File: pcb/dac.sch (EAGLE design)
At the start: 24 parts, among them Q1 2N7000, U1 PIC16F1773-I/SP, U2 MCP6002-I/P

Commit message: Notes on diffusion angle and lighting
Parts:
- removed R3: 220R, rcl:R-US_0207/2V
- added R5, RP: 100R, rcl:R-US_0207/2V
- JPH: device pinhead:PINHD-1X4 -> pinhead:PINHD-1X5
- R1, R2, R4: value 220R -> 100R
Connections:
- new net N$1: JPH.5, RP.2
- net +5V: now also R5.1, RP.1; no longer R3.1
- net LED3: now also R4.2; no longer R3.2
- net LED4: now also R5.2; no longer R4.2
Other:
- note added: "105mA < 200mA"
- note added: "R1-R5: C5xx-Axx amber LEDs Rp: C5xx-Rxx red LED If ~ 21mA < 30mA Vf = 2.1V typ"
- note removed: "53mA < 200mA"
- note removed: "LTL-1CHA amber LEDs If ~ 13mA < 20mA Vf = 2.1V typ"
- moved on the sheet: R4
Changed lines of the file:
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@@
 <?xml version="1.0" encoding="utf-8"?>
 <!DOCTYPE eagle SYSTEM "eagle.dtd">
-<eagle version="9.6.2">
+<eagle version="9.5.2">
 <drawing>
 <settings>
@@
 <part name="GND6" library="supply1" library_urn="urn:adsk.eagle:library:371" deviceset="GND" device=""/>
 <part name="P+4" library="supply1" library_urn="urn:adsk.eagle:library:371" deviceset="+5V" device=""/>
-<part name="R1" library="rcl" library_urn="urn:adsk.eagle:library:334" deviceset="R-US_" device="0207/2V" package3d_urn="urn:adsk.eagle:package:23490/1" value="220R"/>
-<part name="R2" library="rcl" library_urn="urn:adsk.eagle:library:334" deviceset="R-US_" device="0207/2V" package3d_urn="urn:adsk.eagle:package:23490/1" value="220R"/>
-<part name="R3" library="rcl" library_urn="urn:adsk.eagle:library:334" deviceset="R-US_" device="0207/2V" package3d_urn="urn:adsk.eagle:package:23490/1" value="220R"/>
-<part name="R4" library="rcl" library_urn="urn:adsk.eagle:library:334" deviceset="R-US_" device="0207/2V" package3d_urn="urn:adsk.eagle:package:23490/1" value="220R"/>
+<part name="R1" library="rcl" library_urn="urn:adsk.eagle:library:334" deviceset="R-US_" device="0207/2V" package3d_urn="urn:adsk.eagle:package:23490/1" value="100R"/>
+<part name="R2" library="rcl" library_urn="urn:adsk.eagle:library:334" deviceset="R-US_" device="0207/2V" package3d_urn="urn:adsk.eagle:package:23490/1" value="100R"/>
+<part name="R4" library="rcl" library_urn="urn:adsk.eagle:library:334" deviceset="R-US_" device="0207/2V" package3d_urn="urn:adsk.eagle:package:23490/1" value="100R"/>
+<part name="R5" library="rcl" library_urn="urn:adsk.eagle:library:334" deviceset="R-US_" device="0207/2V" package3d_urn="urn:adsk.eagle:package:23490/1" value="100R"/>
 <part name="Q1" library="transistor-fet" library_urn="urn:adsk.eagle:library:396" deviceset="TN0604N3" device="" package3d_urn="urn:adsk.eagle:package:28535/2" value="2N7000"/>
 <part name="GND7" library="supply1" library_urn="urn:adsk.eagle:library:371" deviceset="GND" device=""/>
@@
 <part name="GND10" library="supply1" library_urn="urn:adsk.eagle:library:371" deviceset="GND" device=""/>
 <part name="JPL" library="pinhead" library_urn="urn:adsk.eagle:library:325" deviceset="PINHD-1X3" device="" package3d_urn="urn:adsk.eagle:package:22458/2"/>
-<part name="JPH" library="pinhead" library_urn="urn:adsk.eagle:library:325" deviceset="PINHD-1X4" device="" package3d_urn="urn:adsk.eagle:package:22407/2"/>
+<part name="JPH" library="pinhead" library_urn="urn:adsk.eagle:library:325" deviceset="PINHD-1X5" device="" package3d_urn="urn:adsk.eagle:package:22469/2"/>
 <part name="D1" library="diode" library_urn="urn:adsk.eagle:library:210" deviceset="ZENER-DIODE" device="P1-Z12" package3d_urn="urn:adsk.eagle:package:43340/1" value="SA5.0A"/>
 <part name="JG1H" library="pinhead" library_urn="urn:adsk.eagle:library:325" deviceset="PINHD-1X1" device="" package3d_urn="urn:adsk.eagle:package:22485/2"/>
@@
 <part name="JG5H" library="pinhead" library_urn="urn:adsk.eagle:library:325" deviceset="PINHD-1X1" device="" package3d_urn="urn:adsk.eagle:package:22485/2"/>
 <part name="JG5L" library="pinhead" library_urn="urn:adsk.eagle:library:325" deviceset="PINHD-1X1" device="" package3d_urn="urn:adsk.eagle:package:22485/2"/>
+<part name="RP" library="rcl" library_urn="urn:adsk.eagle:library:334" deviceset="R-US_" device="0207/2V" package3d_urn="urn:adsk.eagle:package:23490/1" value="100R"/>
 </parts>
 <sheets>
@@
 <text x="134.62" y="142.24" size="1.778" layer="97">Connect to something like the Adafruit 206 cable,
 crimp female rectangular cable</text>
-<text x="127" y="92.71" size="1.778" layer="97">LTL-1CHA amber LEDs
-If ~ 13mA &lt; 20mA
+<text x="132.08" y="99.06" size="1.778" layer="97" rot="MR180">R1-R5: C5xx-Axx amber LEDs
+Rp: C5xx-Rxx red LED
+If ~ 21mA &lt; 30mA
 Vf = 2.1V typ</text>
-<text x="109.22" y="100.33" size="1.778" layer="97" rot="MR0">53mA &lt; 200mA</text>
+<text x="109.22" y="100.33" size="1.778" layer="97" rot="MR0">105mA &lt; 200mA</text>
 </plain>
 <instances>
@@
 <attribute name="VALUE" x="150.368" y="121.92" size="1.778" layer="96" rot="R270"/>
 </instance>
-<instance part="R3" gate="G$1" x="153.67" y="120.65" smashed="yes" rot="R270">
+<instance part="R4" gate="G$1" x="153.67" y="120.65" smashed="yes" rot="R270">
 <attribute name="NAME" x="155.1686" y="127" size="1.778" layer="95" rot="R270"/>
 <attribute name="VALUE" x="155.448" y="121.92" size="1.778" layer="96" rot="R270"/>
 </instance>
-<instance part="R4" gate="G$1" x="158.75" y="120.65" smashed="yes" rot="R270">
+<instance part="R5" gate="G$1" x="158.75" y="120.65" smashed="yes" rot="R270">
 <attribute name="NAME" x="160.2486" y="127" size="1.778" layer="95" rot="R270"/>
 <attribute name="VALUE" x="160.528" y="121.92" size="1.778" layer="96" rot="R270"/>
@@
 </instance>
 <instance part="JPL" gate="A" x="128.27" y="110.49" smashed="yes">
-<attribute name="NAME" x="121.92" y="118.745" size="1.778" layer="95"/>
+<attribute name="NAME" x="121.92" y="116.205" size="1.778" layer="95"/>
 <attribute name="VALUE" x="121.92" y="102.87" size="1.778" layer="96"/>
 </instance>
@@
 <attribute name="NAME" x="68.58" y="26.035" size="1.778" layer="95" rot="R180"/>
 <attribute name="VALUE" x="77.47" y="30.48" size="1.778" layer="96" rot="R180"/>
+</instance>
+<instance part="RP" gate="G$1" x="163.83" y="120.65" smashed="yes" rot="R270">
+<attribute name="NAME" x="165.3286" y="127" size="1.778" layer="95" rot="R270"/>
+<attribute name="VALUE" x="165.608" y="121.92" size="1.778" layer="96" rot="R270"/>
 </instance>
 </instances>
@@
 <pinref part="R1" gate="G$1" pin="1"/>
 <wire x1="143.51" y1="128.27" x2="143.51" y2="127" width="0.1524" layer="91"/>
-<pinref part="R4" gate="G$1" pin="1"/>
+<pinref part="R5" gate="G$1" pin="1"/>
 <wire x1="143.51" y1="127" x2="143.51" y2="125.73" width="0.1524" layer="91"/>
 <wire x1="158.75" y1="125.73" x2="158.75" y2="127" width="0.1524" layer="91"/>
@@
 <wire x1="148.59" y1="125.73" x2="148.59" y2="127" width="0.1524" layer="91"/>
 <junction x="148.59" y="127"/>
-<pinref part="R3" gate="G$1" pin="1"/>
+<pinref part="R4" gate="G$1" pin="1"/>
 <wire x1="153.67" y1="125.73" x2="153.67" y2="127" width="0.1524" layer="91"/>
 <junction x="153.67" y="127"/>
+<pinref part="RP" gate="G$1" pin="1"/>
+<wire x1="163.83" y1="125.73" x2="163.83" y2="127" width="0.1524" layer="91"/>
+<wire x1="163.83" y1="127" x2="158.75" y2="127" width="0.1524" layer="91"/>
+<junction x="158.75" y="127"/>
 </segment>
 <segment>
@@
 <net name="LED3" class="0">
 <segment>
-<pinref part="R3" gate="G$1" pin="2"/>
+<pinref part="R4" gate="G$1" pin="2"/>
 <wire x1="153.67" y1="115.57" x2="153.67" y2="107.95" width="0.1524" layer="91"/>
 <wire x1="153.67" y1="107.95" x2="135.89" y2="107.95" width="0.1524" layer="91"/>
@@
 <net name="LED4" class="0">
 <segment>
-<pinref part="R4" gate="G$1" pin="2"/>
+<pinref part="R5" gate="G$1" pin="2"/>
 <wire x1="158.75" y1="115.57" x2="158.75" y2="105.41" width="0.1524" layer="91"/>
 <wire x1="158.75" y1="105.41" x2="135.89" y2="105.41" width="0.1524" layer="91"/>
@@
 <segment>
 <pinref part="Q1" gate="G$1" pin="D"/>
-<wire x1="119.38" y1="101.6" x2="119.38" y2="105.41" width="0.1524" layer="91"/>
+<wire x1="119.38" y1="101.6" x2="119.38" y2="102.87" width="0.1524" layer="91"/>
+<wire x1="119.38" y1="102.87" x2="119.38" y2="105.41" width="0.1524" layer="91"/>
 <wire x1="119.38" y1="105.41" x2="119.38" y2="107.95" width="0.1524" layer="91"/>
 <wire x1="119.38" y1="107.95" x2="119.38" y2="110.49" width="0.1524" layer="91"/>
@@
 <junction x="127" y="105.41"/>
 <label x="118.11" y="110.49" size="1.778" layer="95" rot="MR0"/>
+<wire x1="119.38" y1="102.87" x2="127" y2="102.87" width="0.1524" layer="91"/>
+<junction x="119.38" y="102.87"/>
+<junction x="127" y="102.87"/>
 </segment>
 </net>
@@
 </segment>
 </net>
+<net name="N$1" class="0">
+<segment>
+<pinref part="JPH" gate="A" pin="5"/>
+<pinref part="RP" gate="G$1" pin="2"/>
+<wire x1="135.89" y1="102.87" x2="163.83" y2="102.87" width="0.1524" layer="91"/>
+<wire x1="163.83" y1="102.87" x2="163.83" y2="115.57" width="0.1524" layer="91"/>
+</segment>
+</net>

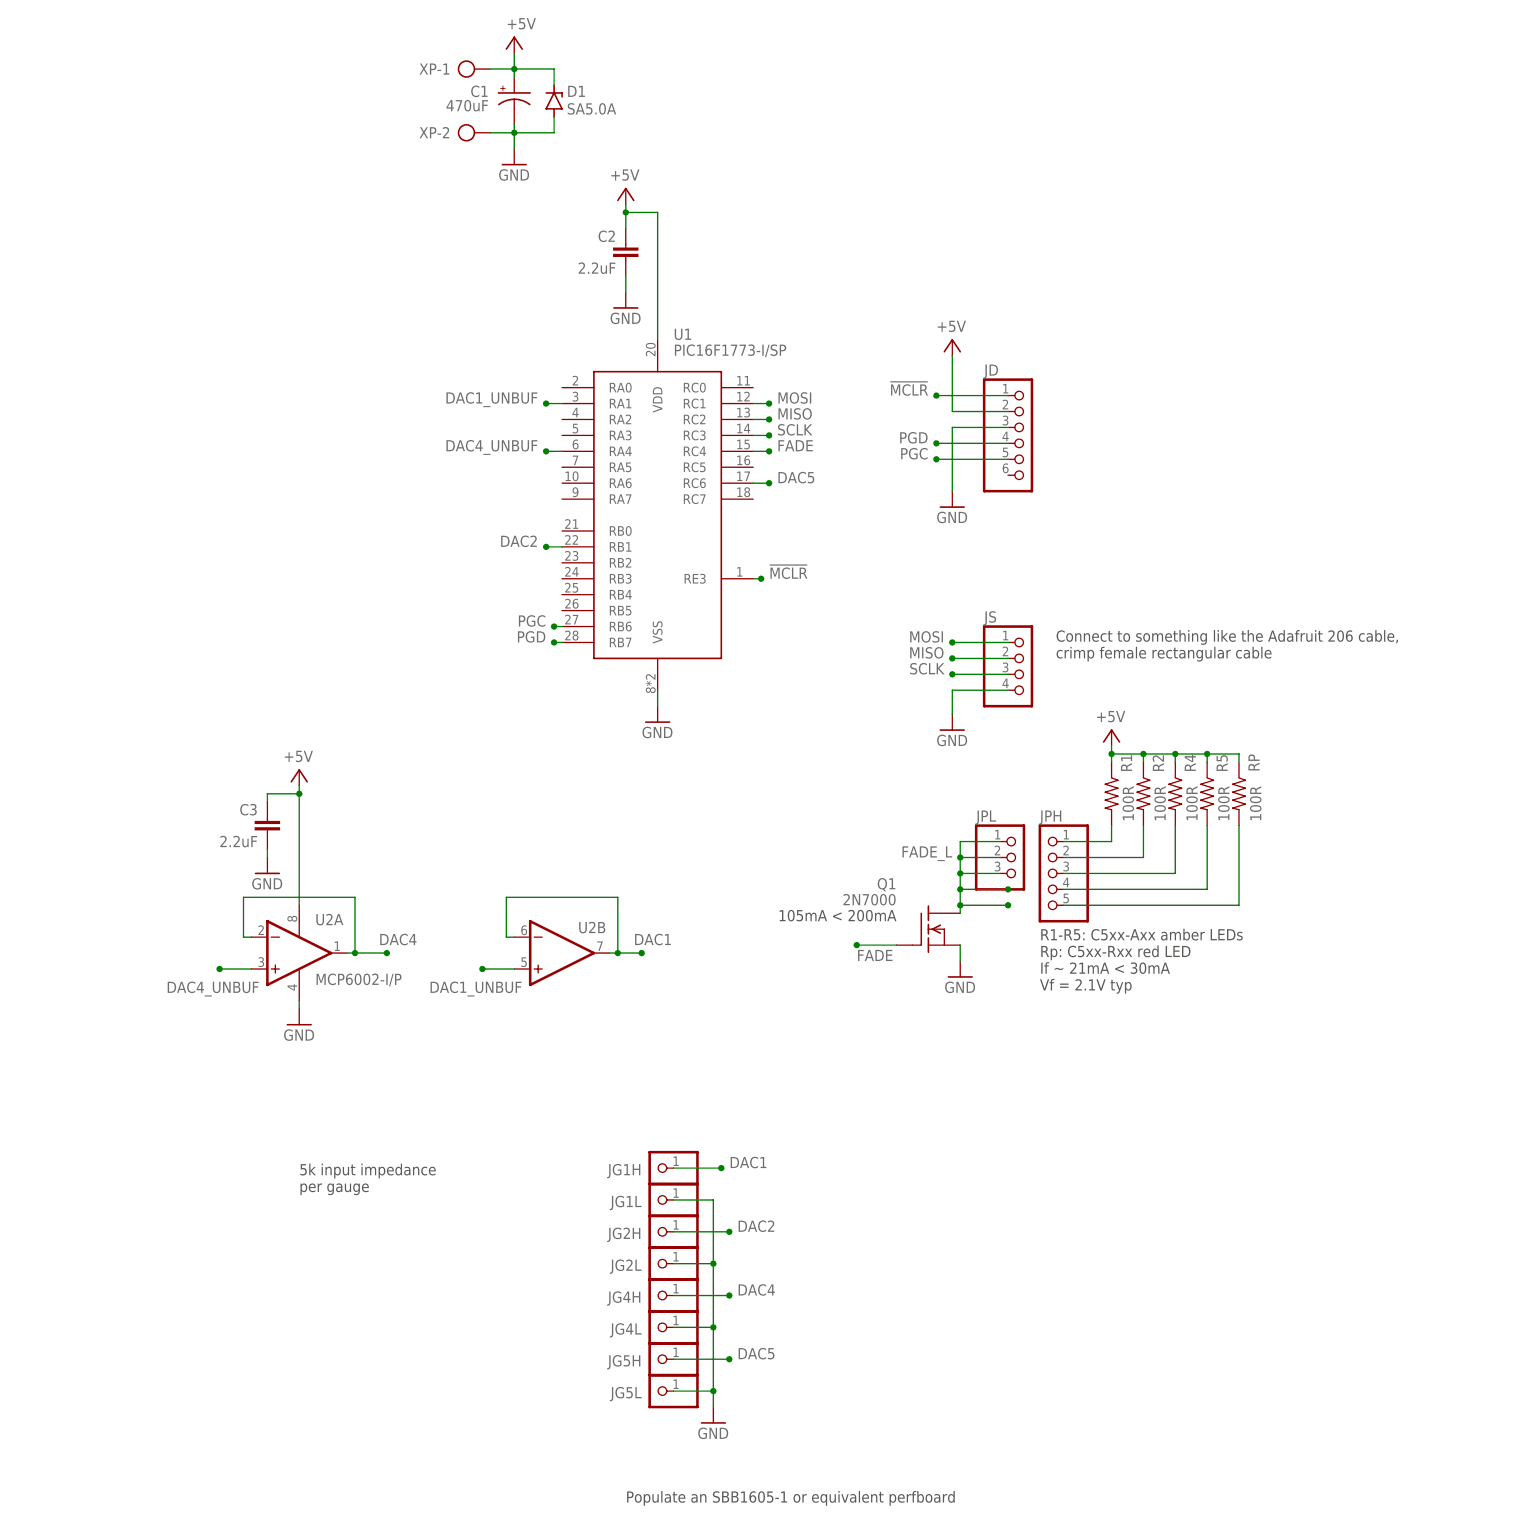
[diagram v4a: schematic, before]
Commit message: MISO pullup, minor cleanup
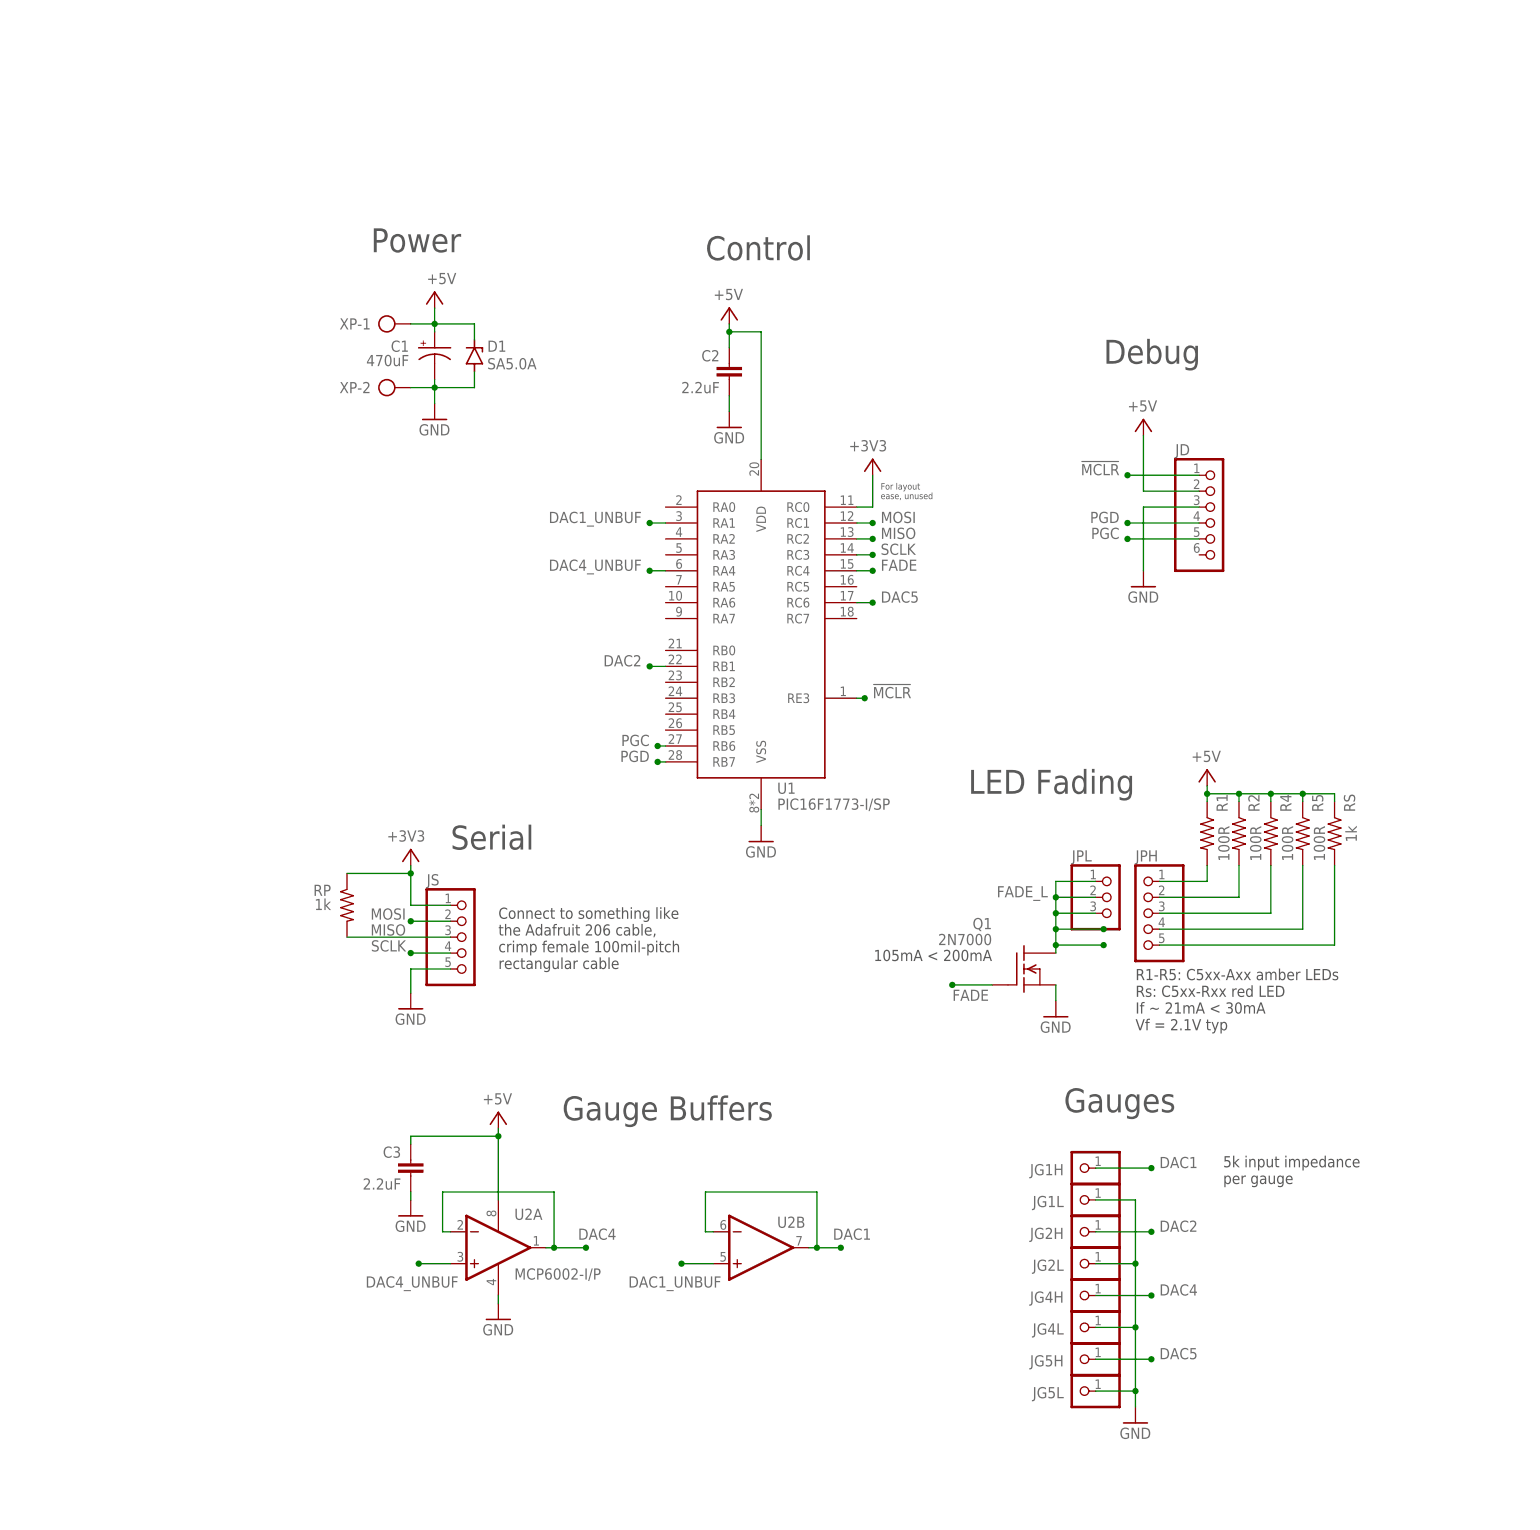
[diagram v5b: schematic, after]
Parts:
- added RS: 1k, rcl:R-US_0207/2V
- D1: device diode:ZENER-DIODEP1-Z12 -> diode:1N821
- JS: device pinhead:PINHD-1X4 -> pinhead:PINHD-1X5
- RP: value 100R -> 1k; device rcl:R-US_0207/2V -> rcl:R-US_0207/5V
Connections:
- removed net LED3: JPH.3, R4.2
- removed net N$1: JPH.5, RP.2
- new net +3V3: JS.1, RP.1, U1.RC0
- new net LED5: JPH.4, R5.2
- new net LEDSUP: JPH.5, RS.2
- net +5V: now also RS.1; no longer RP.1
- net GND: now also JS.5; no longer JS.4
- net LED4: now also JPH.3, R4.2; no longer JPH.4, R5.2
- net MISO: now also JS.3, RP.2; no longer JS.2
- net MOSI: now also JS.2; no longer JS.1
- net SCLK: now also JS.4; no longer JS.3
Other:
- note added: "Connect to something like the Adafruit 206 cable, crimp female 100mil-pitch rectangular cable"
- note added: "Control"
- note added: "Debug"
- note added: "For layout ease, unused"
- note added: "Gauge Buffers"
- note added: "Gauges"
- note added: "LED Fading"
- note added: "Power"
- note added: "R1-R5: C5xx-Axx amber LEDs Rs: C5xx-Rxx red LED If ~ 21mA < 30mA Vf = 2.1V typ"
- note added: "Serial"
- note removed: "Connect to something like the Adafruit 206 cable, crimp female rectangular cable"
- note removed: "Populate an SBB1605-1 or equivalent perfboard"
- note removed: "R1-R5: C5xx-Axx amber LEDs Rp: C5xx-Rxx red LED If ~ 21mA < 30mA Vf = 2.1V typ"
- moved on the sheet: C1, C2, C3, JD, JG1H, JG1L, JG2H, JG2L, JG4H, JG4L, JG5H, JG5L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

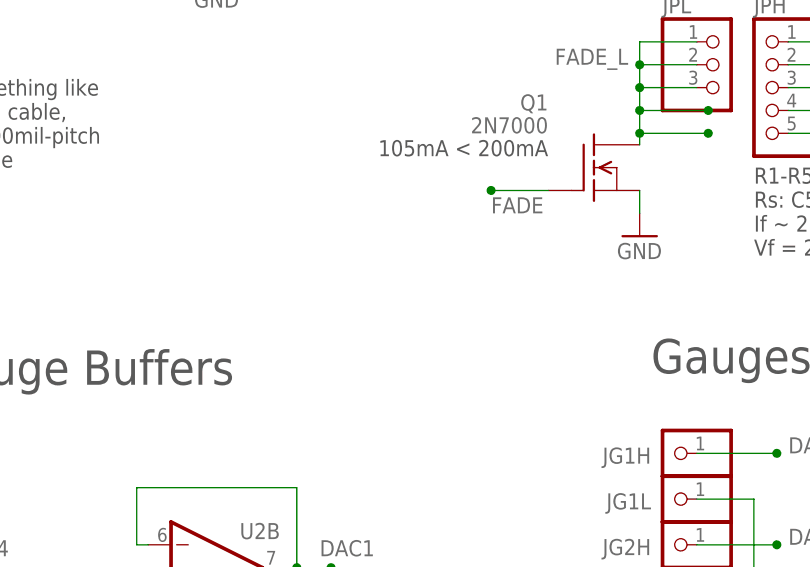
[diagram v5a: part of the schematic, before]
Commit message: Add note about high driving
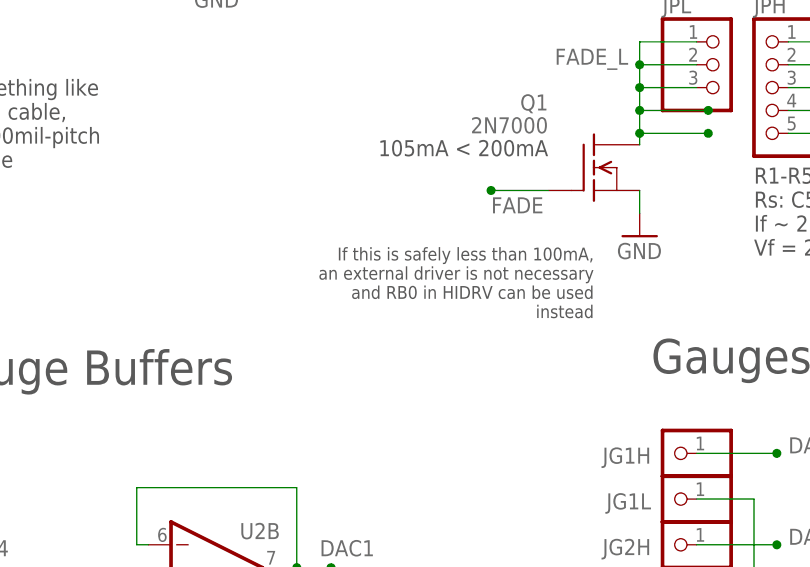
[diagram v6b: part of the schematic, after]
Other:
- note added: "If this is safely less than 100mA, an external driver is not necessary and RB0 in HIDRV can be used instead"
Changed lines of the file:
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@@
 <text x="25.4" y="207.01" size="3.81" layer="97">Power</text>
 <text x="78.74" y="205.74" size="3.81" layer="97">Control</text>
+<text x="129.54" y="83.82" size="1.4224" layer="97" rot="R180">If this is safely less than 100mA,
+an external driver is not necessary
+and RB0 in HIDRV can be used
+instead</text>
 </plain>
 <instances>
